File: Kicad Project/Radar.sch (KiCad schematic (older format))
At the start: 0 parts

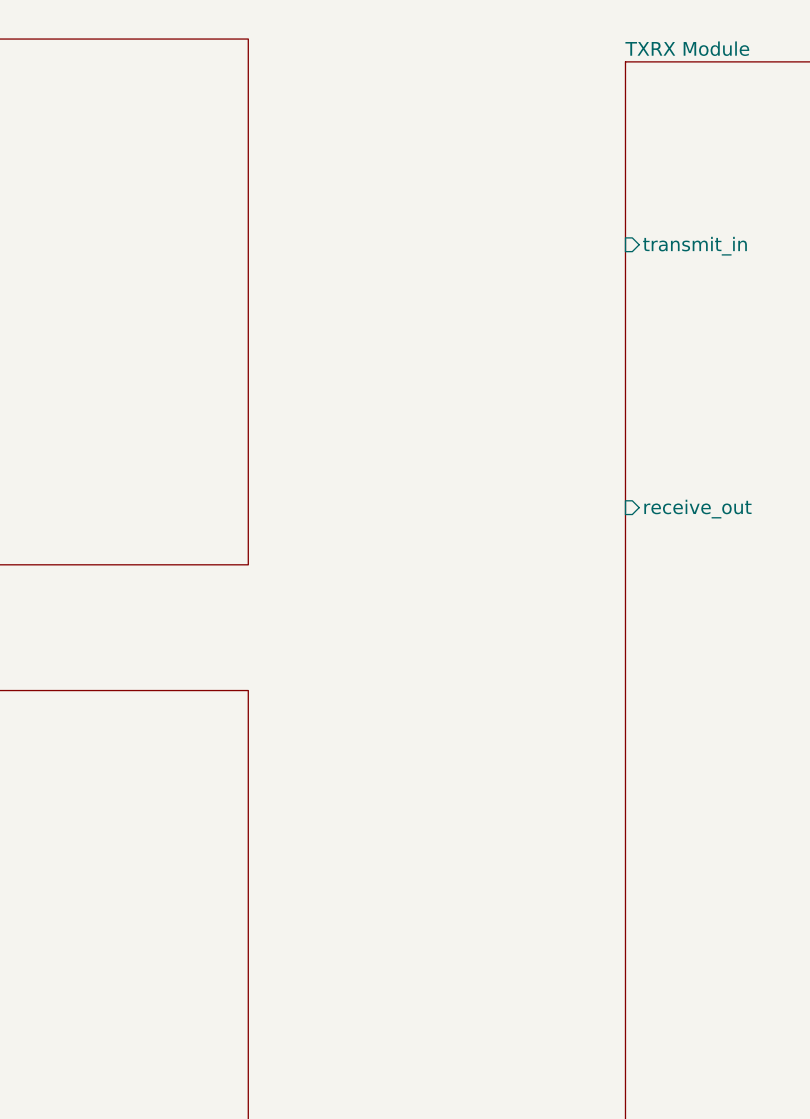
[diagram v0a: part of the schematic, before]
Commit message: PCB for source Module mostly complete, missing filter. Power Spliter still has issues.
Some minor changes made to all schematics for the net lists to be properall connected

A bunch of parts made
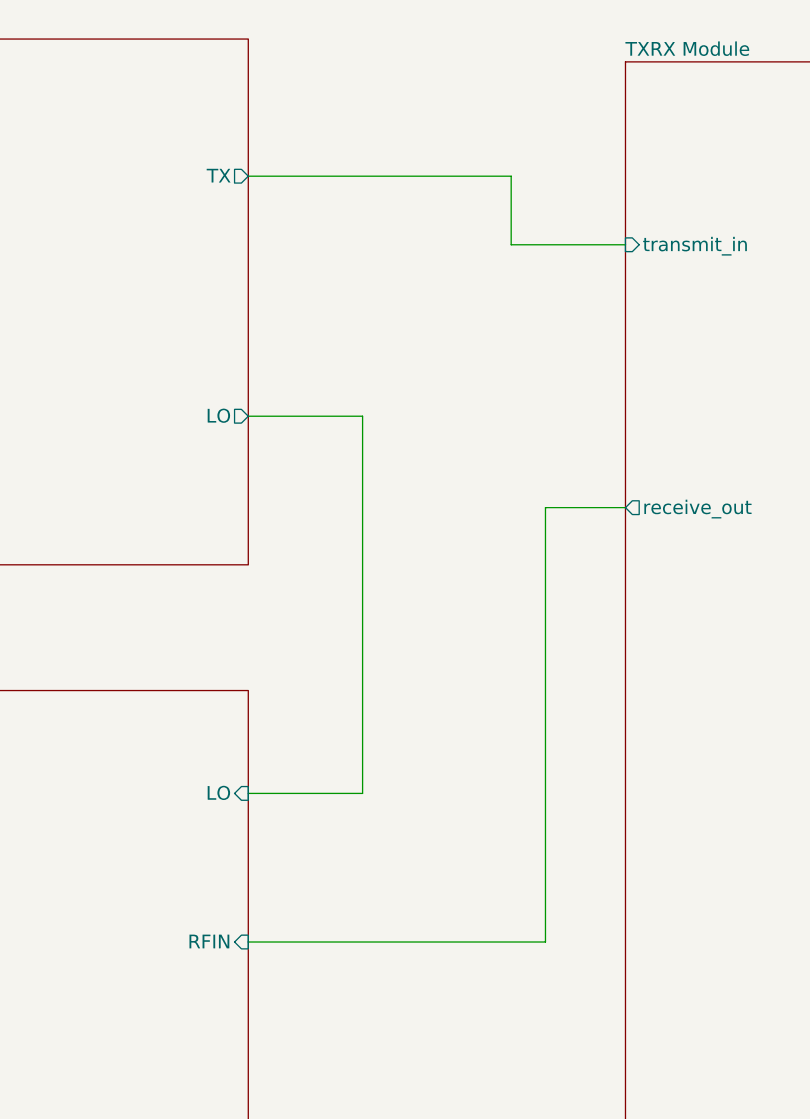
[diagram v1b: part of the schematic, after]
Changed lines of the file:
@@
 F0 "SourceModule.sch" 60
 F1 "SourceModule.sch" 60
+F2 "TX" O R 7050 2900 60
+F3 "LO" O R 7050 3950 60
 $EndSheet
 $Sheet
@@
 F1 "TXRX Module.sch" 60
 F2 "transmit_in" I L 8700 3200 60
-F3 "receive_out" I L 8700 4350 60
+F3 "receive_out" O L 8700 4350 60
 $EndSheet
 $Sheet
@@
 F0 "DownconverterPreampModule" 60
 F1 "DownconverterPreampModule.sch" 60
+F2 "LO" I R 7050 5600 60
+F3 "RFIN" I R 7050 6250 60
 $EndSheet
+Wire Wire Line
+	7050 6250 8350 6250
+Wire Wire Line
+	8350 6250 8350 4350
+Wire Wire Line
+	8350 4350 8700 4350
+Wire Wire Line
+	7050 3950 7550 3950
+Wire Wire Line
+	7550 3950 7550 5600
+Wire Wire Line
+	7550 5600 7050 5600
+Wire Wire Line
+	7050 2900 8200 2900
+Wire Wire Line
+	8200 2900 8200 3200
+Wire Wire Line
+	8200 3200 8700 3200
 $EndSCHEMATC
